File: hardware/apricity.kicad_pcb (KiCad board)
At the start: 2 copper layers, 71.2 x 71.2 mm, 26 parts, among them J1 USB_C_Receptacle_USB2.0, U1 ESP-WROOM-02D, U2 X

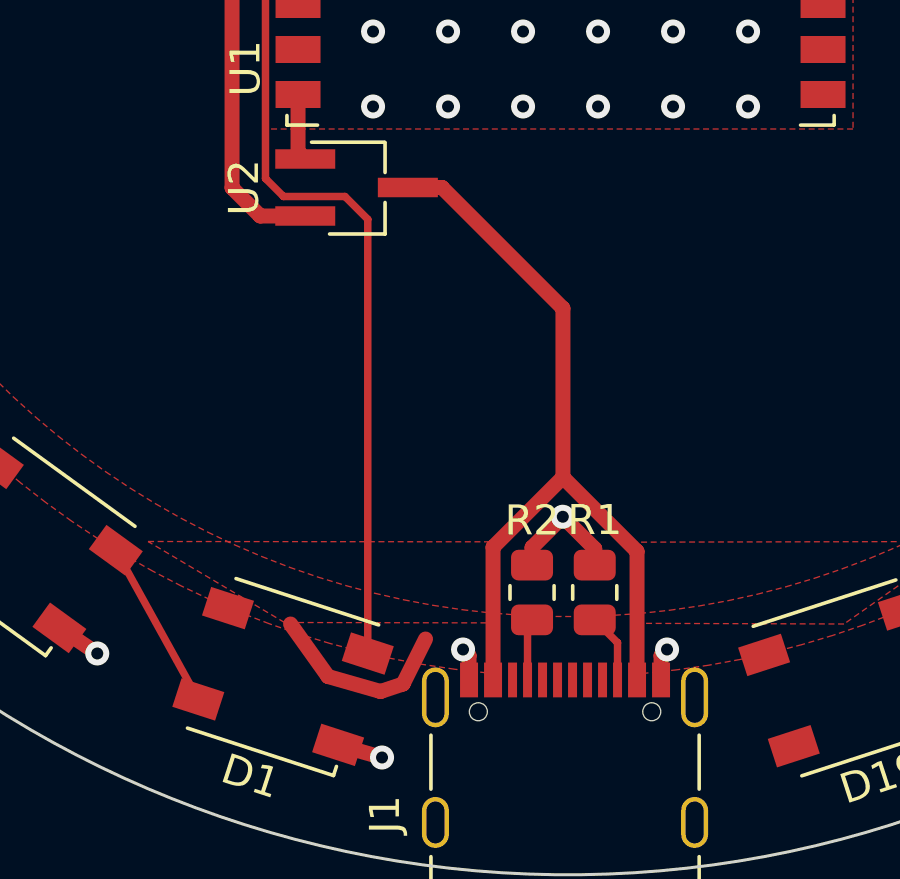
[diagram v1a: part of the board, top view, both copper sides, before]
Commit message: use jumper to connect power trace
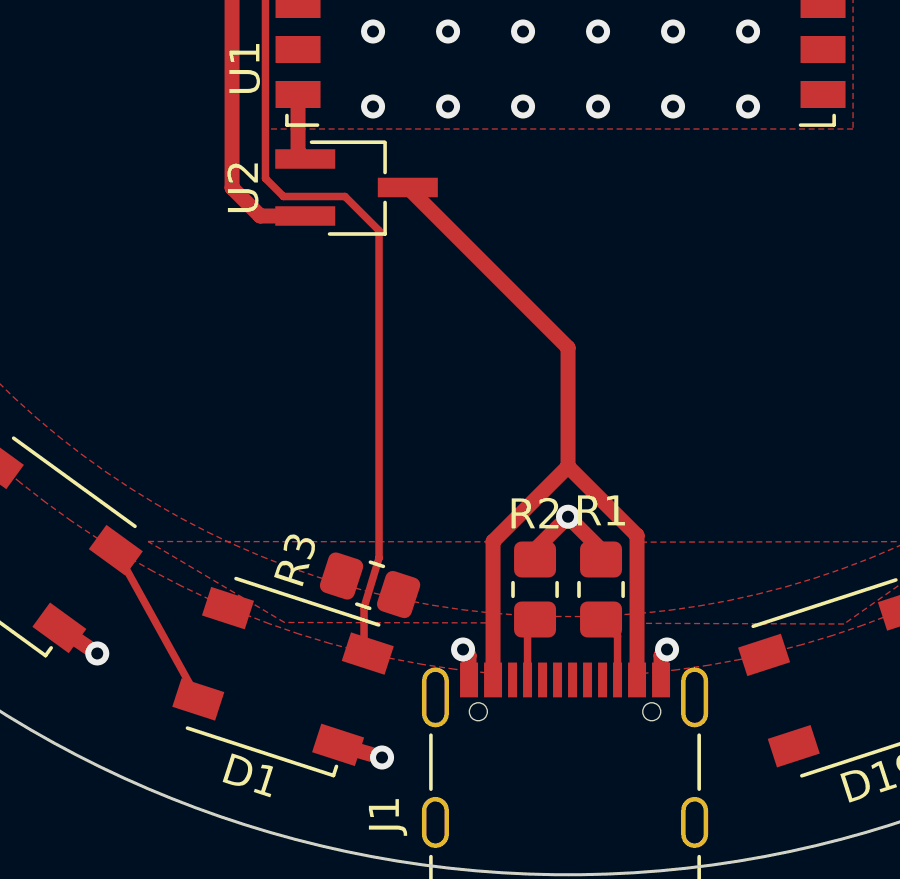
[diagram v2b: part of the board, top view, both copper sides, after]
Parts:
- added R3: 0, Resistor_SMD:R_0805_2012Metric_Pad1.20x1.40mm_HandSolder, F.Cu at (141.4, 120.0)
- R1, R2: footprint Resistor_SMD:R_0805_2012Metric -> Resistor_SMD:R_0805_2012Metric_Pad1.20x1.40mm_HandSolder
- moved R1 0.23 mm to (149.1, 120.1)
- moved R2 0.14 mm to (146.9, 120.1)
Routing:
- net +5V: track 34.4 -> 27.7 mm

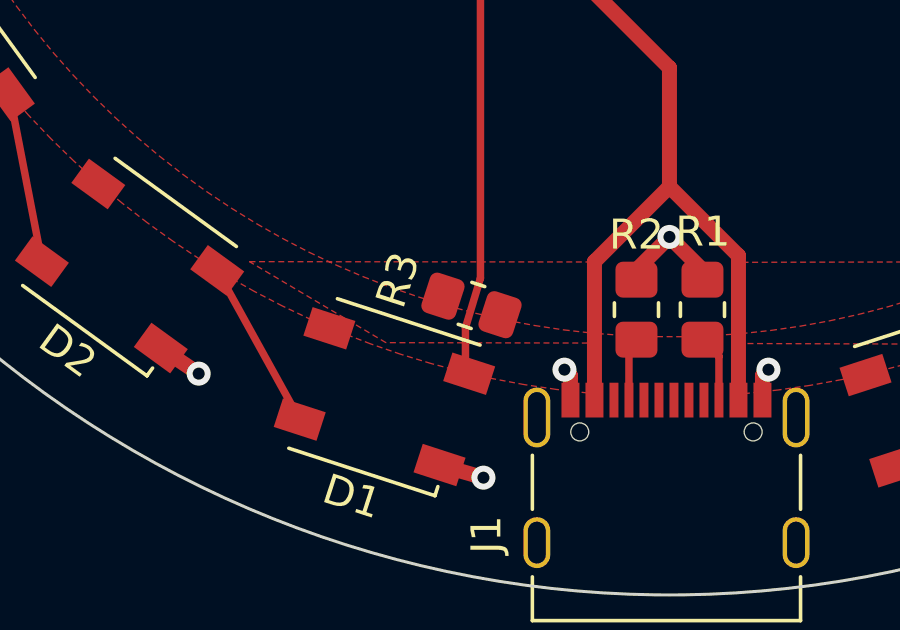
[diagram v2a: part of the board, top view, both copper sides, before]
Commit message: fix routing issues with jumper
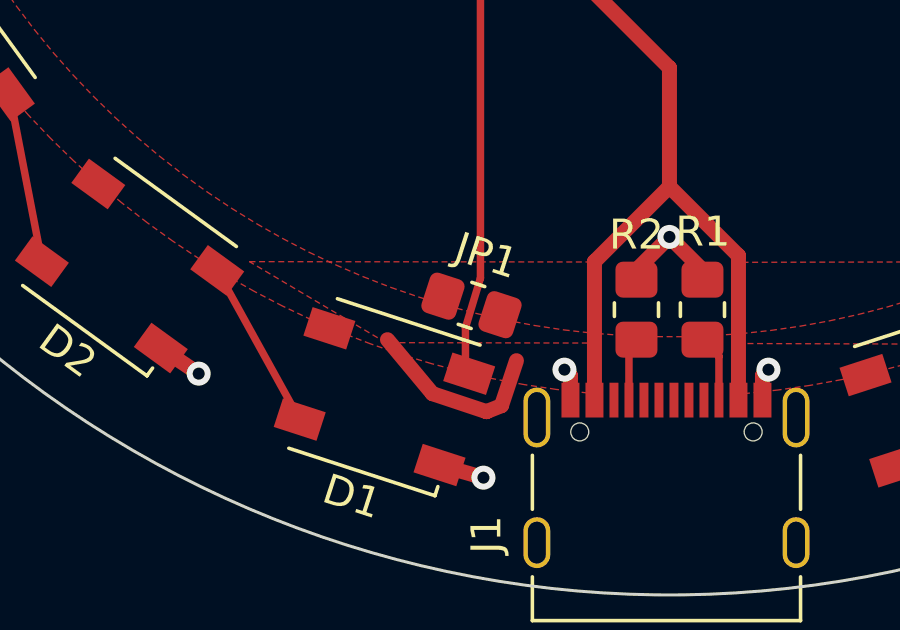
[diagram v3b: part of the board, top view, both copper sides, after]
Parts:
- JP1: renamed from R3; value 0 -> SolderJumper_2_Bridged
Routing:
- net +5V: track 27.7 -> 34.1 mm
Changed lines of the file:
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@@
     (property "Sheetname" "")
     (attr smd)
-    (fp_text reference "R3" (at 2.592753 0.051306 252) (layer "F.SilkS")
-      (effects (font (size 1 1) (thickness 0.15)))
-    )
-    (fp_text value "0" (at 0 1.65 162) (layer "F.Fab")
+    (fp_text reference "JP1" (at 0.038141 1.732001 342) (layer "F.SilkS")
+      (effects (font (size 1 1) (thickness 0.15)))
+    )
+    (fp_text value "SolderJumper_2_Bridged" (at 0 1.65 162) (layer "F.Fab")
       (effects (font (size 1 1) (thickness 0.15)))
     )
@@
     (fp_line (start -1 -0.625) (end 1 -0.625) (layer "F.Fab") (width 0.1))
     (pad "1" smd roundrect (at -1 0 162) (size 1.2 1.4) (layers "F.Cu" "F.Paste" "F.Mask") (roundrect_rratio 0.208333)
-      (net 2 "+5V") (pintype "passive"))
+      (net 2 "+5V") (pinfunction "A") (pintype "passive"))
     (pad "2" smd roundrect (at 1 0 162) (size 1.2 1.4) (layers "F.Cu" "F.Paste" "F.Mask") (roundrect_rratio 0.208333)
-      (net 2 "+5V") (pintype "passive"))
+      (net 2 "+5V") (pinfunction "B") (pintype "passive"))
     (model "${KICAD6_3DMODEL_DIR}/Resistor_SMD.3dshapes/R_0805_2012Metric.wrl"
       (offset (xyz 0 0 0))
@@
   (segment (start 145.5 118.5) (end 148 116) (width 0.5) (layer "F.Cu") (net 2))
   (segment (start 150.3 123.115) (end 150.3 118.3) (width 0.5) (layer "F.Cu") (net 2))
+  (segment (start 140.1 122.9) (end 138.6 121.1) (width 0.5) (layer "F.Cu") (net 2))
+  (segment (start 142.9 121.8) (end 142.4 123.3) (width 0.5) (layer "F.Cu") (net 2))
   (segment (start 145.5 123.115) (end 145.5 118.5) (width 0.5) (layer "F.Cu") (net 2))
+  (segment (start 141.9 123.5) (end 140.1 122.9) (width 0.5) (layer "F.Cu") (net 2))
+  (segment (start 142.4 123.3) (end 141.9 123.5) (width 0.5) (layer "F.Cu") (net 2))
   (segment (start 150.3 118.3) (end 148 116) (width 0.5) (layer "F.Cu") (net 2))
   (segment (start 137.915 106.4) (end 138.515 107) (width 0.25) (layer "F.Cu") (net 3))
